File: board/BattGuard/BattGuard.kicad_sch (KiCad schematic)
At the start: 157 parts, among them J1 OQ0271510000G, J10 Conn_01x01_Pin, J11 Conn_01x01_Pin, J12 Conn_01x01_Pin, J13 Conn_01x01_Pin, J14 Conn_01x01_Pin, J15 Conn_01x01_Pin, J17 S5B-XH-A, J2 Barrel_Jack, J3 Conn_01x22_Pin, J4 Conn_01x22_Pin, J5 Conn_01x02_Pin(xt60), J6 OLED DISPLAY, J7 EC5 JUMP CONNECTOR, J8 GSB4111312HR, J9 Conn_01x01_Pin, Q1 SIR680LDP-T1-RE3, Q2 SIR680LDP-T1-RE3, Q3 SIR680LDP-T1-RE3, Q4 SIR680LDP-T1-RE3, Q7 AO3401A, Q8 2N7002, Q9 AO3401A, SW1 SW_Push, SW2 SW_Push, U1 BQ25756ERRVR, U2 LMR51420XDDCR, U3 MCP45HV51-ST, U4 INA226, U5 LM317_TO3, U6 TLV76133KVUR, U7 TLV61047DDC

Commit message: 10.19.2026 v2
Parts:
- removed Q9: AO3401A, Package_TO_SOT_SMD:SOT-23, symbol Transistor_FET:AO3401A
- removed R20: 100k, Resistor_SMD:R_0805_2012Metric, symbol Device:R_US
- D10, D11, D7, D8, D9: footprint TestPoint:TestPoint_Pad_1.0x1.0mm -> LED_THT:LED_D1.8mm_W1.8mm_H2.4mm_Horizontal_O1.27mm_Z4.9mm
- R19: value 100 -> 1k
- R21: value 100k -> 1K
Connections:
- net GPIO4: now also Q8.1 (G), R19.2; no longer R19.1
- net at Q7.2 (S), R21.1: now also R18.1, U5.3 (VO)
- net at C42.1, R22.1, U4.10 (Vin+): now also Q7.3 (D)
- net -BATT renamed GND
- net GND: now also R19.1
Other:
- moved on the sheet: C42, Q8, R19

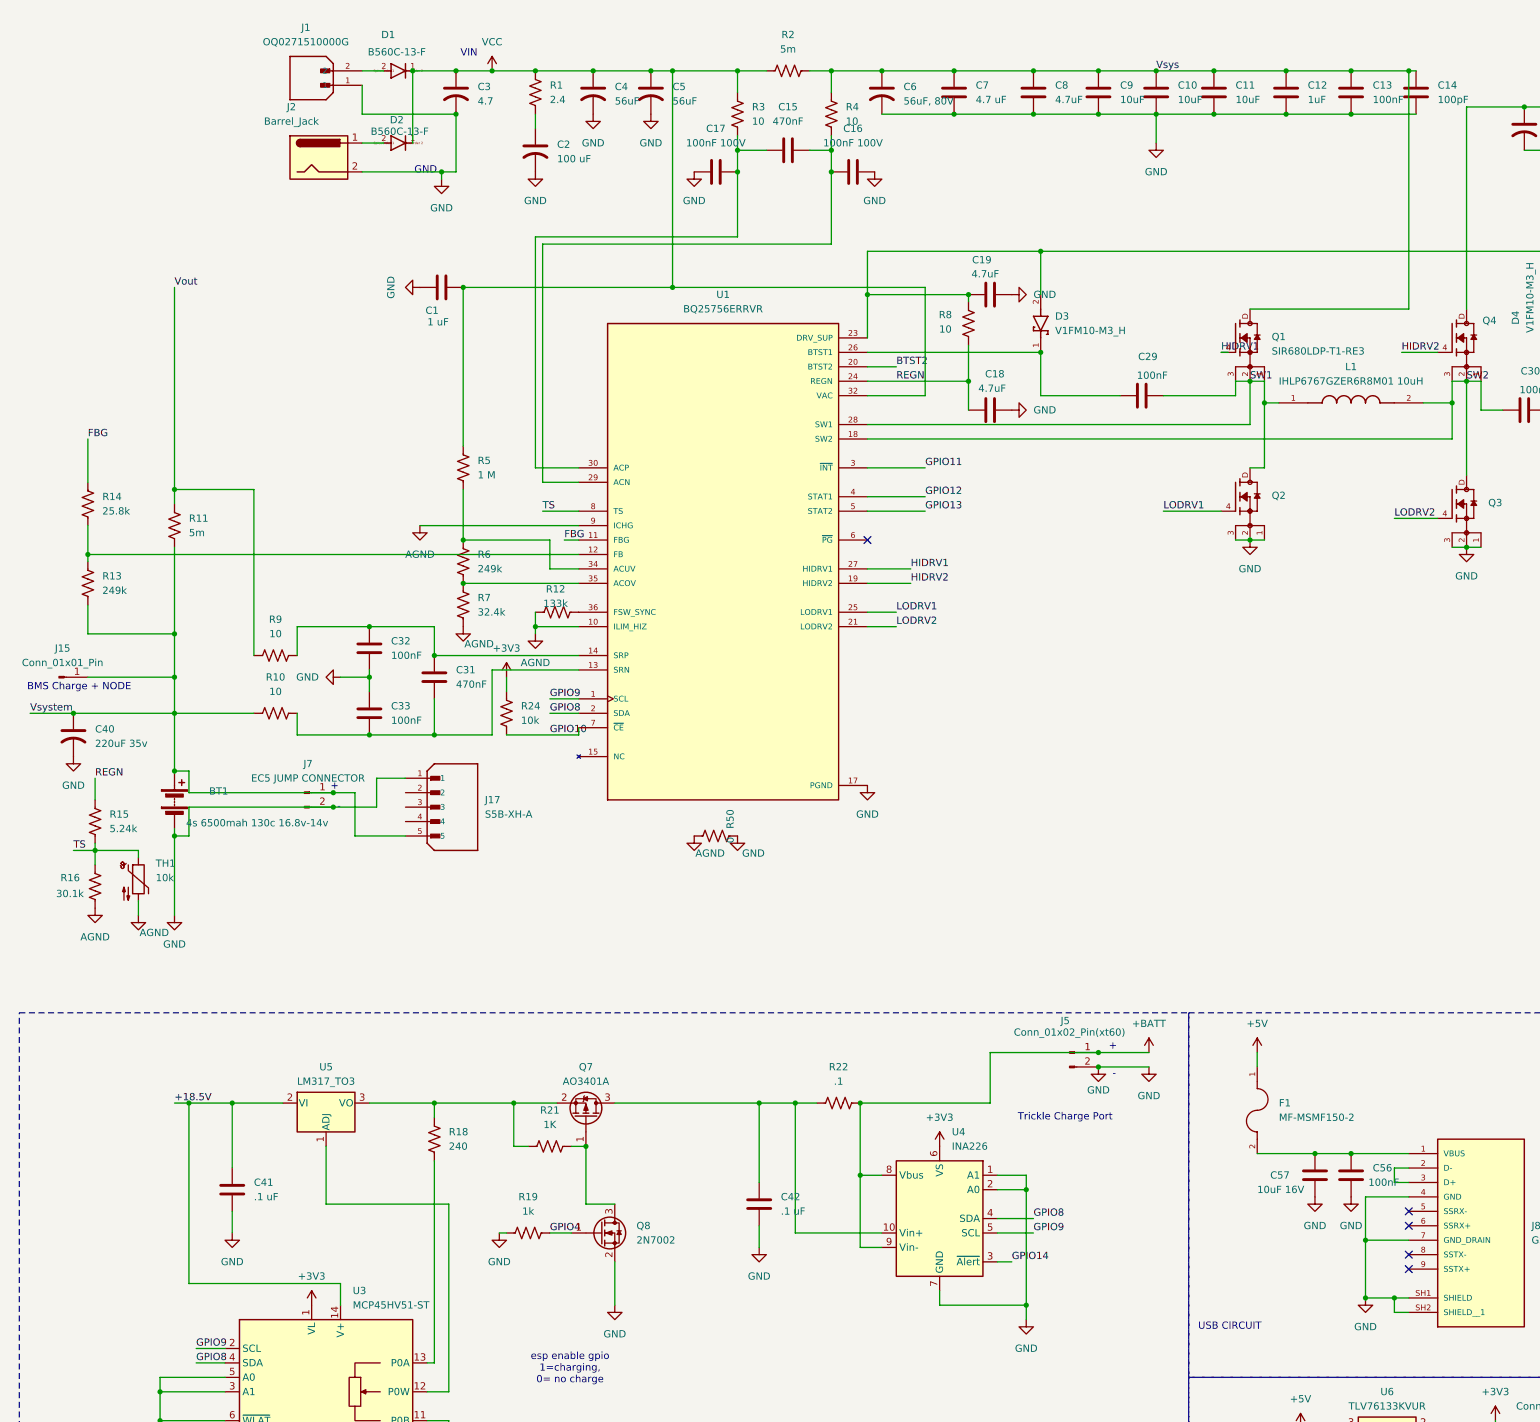
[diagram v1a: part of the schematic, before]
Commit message: Updated ESP32 Devkit, Added Input protection
Reverse polarity BQ Input protection, labeled input blocks, added model for U2
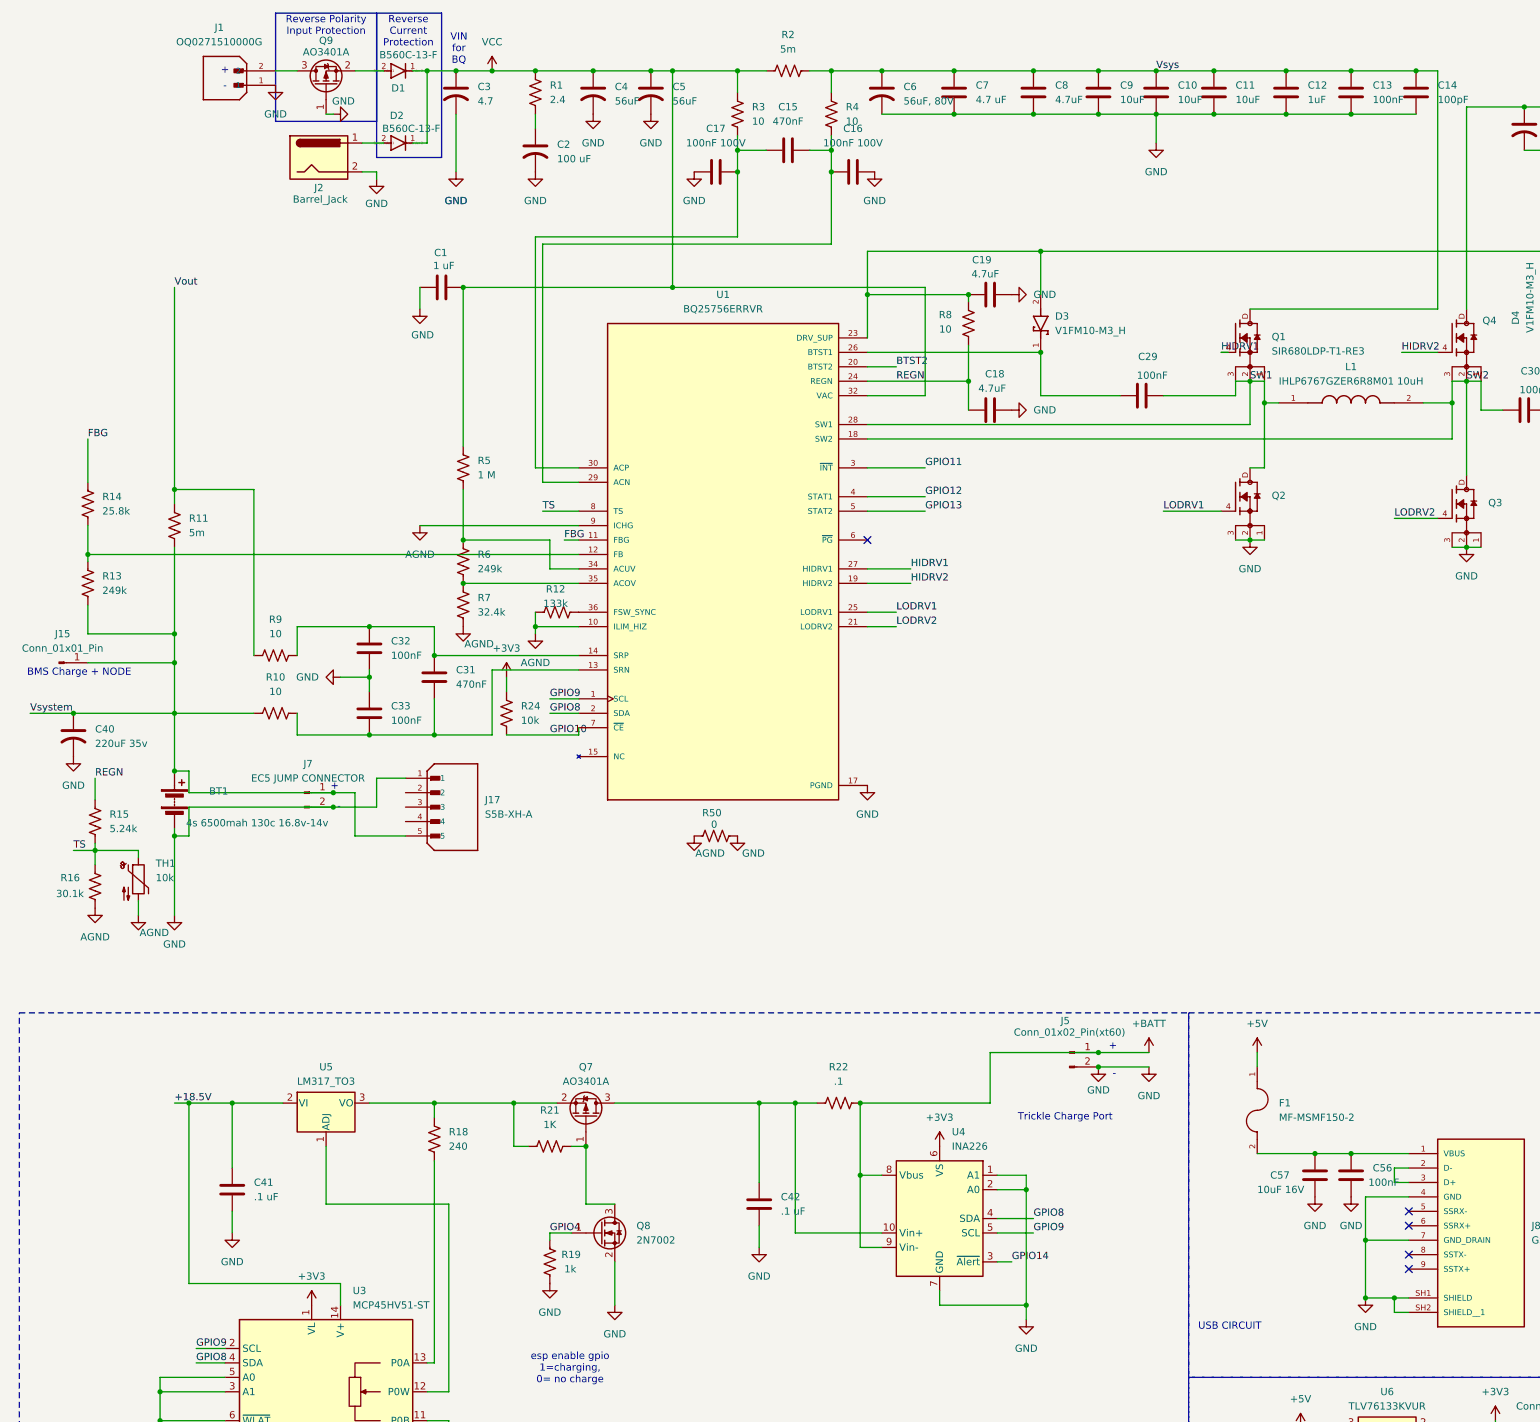
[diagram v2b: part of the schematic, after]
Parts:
- added Q9: AO3401A, Package_TO_SOT_SMD:SOT-23, symbol Transistor_FET:AO3401A
- J1: footprint BattGuard:CONN_SD-39522-003_02P_MOL -> Connector_Phoenix_GMSTB:PhoenixContact_GMSTBA_2,5_2-G_1x02_P7.50mm_Horizontal
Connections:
- net GND: now also Q9.1 (G)
- net at D1.2: now also Q9.2 (S); no longer J1.2
- new net: J1.2, Q9.3 (D)
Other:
- note added: "Reverse Current Protection"
- note added: "Reverse Polarity Input Protection"
- note added: "VIN for BQ"
- note removed: "VIN"
- moved on the sheet: J1, J15, R19

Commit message: 10.20.2026 Changes
Fixed connectors, pours, some NCs
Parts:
- R22: value .1 -> 0.05
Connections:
- net GPIO11: no longer J3.18 (Pin_18), J3.19 (Pin_19), J3.20 (Pin_20), R26.2, R27.2, R28.2, U1.4 (STAT1), U1.5 (STAT2), U4.3 (~{Alert})
- net VCC: now reaches J1.2, Q9.3 (D)
- new net GPIO12: J3.18 (Pin_18), R26.2, U1.4 (STAT1)
- new net GPIO13: J3.19 (Pin_19), R27.2, U1.5 (STAT2)
- new net GPIO14: J3.20 (Pin_20), R28.2, U4.3 (~{Alert})
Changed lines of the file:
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@@
 	(text "USB CIRCUIT\n"
 		(exclude_from_sim no)
-		(at 225.044 243.84 0)
+		(at 225.044 250.444 0)
 		(effects
 			(font
@@
 	)
 	(junction
-		(at 306.07 115.57)
-		(diameter 0)
-		(color 0 0 0 0)
-	)
-	(junction
 		(at 127 22.86)
 		(diameter 0)
@@
 	)
 	(junction
-		(at 306.07 113.03)
-		(diameter 0)
-		(color 0 0 0 0)
-	)
-	(junction
 		(at 67.31 149.86)
 		(diameter 0)
@@
 	)
 	(junction
-		(at 95.25 22.86)
-		(diameter 0)
-		(color 0 0 0 0)
-	)
-	(junction
 		(at 298.45 95.25)
 		(diameter 0)
@@
 	)
 	(junction
-		(at 306.07 110.49)
+		(at 58.42 22.86)
 		(diameter 0)
 		(color 0 0 0 0)
@@
 	)
 	(junction
-		(at 306.07 107.95)
-		(diameter 0)
-		(color 0 0 0 0)
-	)
-	(junction
 		(at 176.53 30.48)
 		(diameter 0)
@@
 	(wire
 		(pts
-			(xy 95.25 22.86) (xy 102.87 22.86)
-		)
-		(stroke
-			(width 0)
-			(type default)
-		)
-	)
-	(wire
-		(pts
 			(xy 389.89 78.74) (xy 375.92 78.74)
 		)
@@
 	(wire
 		(pts
-			(xy 306.07 113.03) (xy 306.07 115.57)
-		)
-		(stroke
-			(width 0)
-			(type default)
-		)
-	)
-	(wire
-		(pts
 			(xy 356.87 226.06) (xy 383.54 226.06)
 		)
@@
 	(wire
 		(pts
-			(xy 57.15 22.86) (xy 60.96 22.86)
+			(xy 57.15 22.86) (xy 58.42 22.86)
 		)
 		(stroke
@@
 	(wire
 		(pts
-			(xy 306.07 110.49) (xy 306.07 113.03)
-		)
-		(stroke
-			(width 0)
-			(type default)
-		)
-	)
-	(wire
-		(pts
 			(xy 109.22 212.09) (xy 111.76 212.09)
 		)
@@
 	(wire
 		(pts
-			(xy 88.9 22.86) (xy 95.25 22.86)
+			(xy 88.9 22.86) (xy 102.87 22.86)
 		)
 		(stroke
@@
 	(wire
 		(pts
-			(xy 36.83 252.73) (xy 36.83 255.27)
+			(xy 58.42 22.86) (xy 60.96 22.86)
 		)
 		(stroke
@@
 	(wire
 		(pts
-			(xy 373.38 194.31) (xy 379.73 194.31)
+			(xy 36.83 252.73) (xy 36.83 255.27)
 		)
 		(stroke
@@
 	(wire
 		(pts
-			(xy 269.24 77.47) (xy 269.24 82.55)
+			(xy 373.38 194.31) (xy 379.73 194.31)
 		)
 		(stroke
@@
 	(wire
 		(pts
-			(xy 160.02 217.17) (xy 163.83 217.17)
+			(xy 269.24 77.47) (xy 269.24 82.55)
 		)
 		(stroke
@@
 	(wire
 		(pts
-			(xy 401.32 194.31) (xy 397.51 194.31)
+			(xy 160.02 217.17) (xy 163.83 217.17)
 		)
 		(stroke
@@
 	(wire
 		(pts
-			(xy 68.58 240.03) (xy 68.58 236.22)
+			(xy 401.32 194.31) (xy 397.51 194.31)
 		)
 		(stroke
@@
 	(wire
 		(pts
-			(xy 306.07 107.95) (xy 306.07 110.49)
+			(xy 68.58 240.03) (xy 68.58 236.22)
 		)
 		(stroke
@@
 	)
 	(symbol
-		(lib_id "power:VCC")
-		(at 95.25 22.86 0)
-		(unit 1)
-		(body_style 1)
-		(exclude_from_sim no)
-		(in_bom yes)
-		(on_board yes)
-		(in_pos_files yes)
-		(dnp no)
-		(fields_autoplaced yes)
-		(property "Reference" "#PWR032"
-			(at 95.25 26.67 0)
-			(hide yes)
-			(show_name no)
-			(do_not_autoplace no)
-			(effects
-				(font
-					(size 1.27 1.27)
-				)
-			)
-		)
-		(property "Value" "VCC"
-			(at 95.25 17.78 0)
-			(show_name no)
-			(do_not_autoplace no)
-			(effects
-				(font
-					(size 1.27 1.27)
-				)
-			)
-		)
-		(property "Footprint" ""
-			(at 95.25 22.86 0)
-			(hide yes)
-			(show_name no)
-			(do_not_autoplace no)
-			(effects
-				(font
-					(size 1.27 1.27)
-				)
-			)
-		)
-		(property "Datasheet" ""
-			(at 95.25 22.86 0)
-			(hide yes)
-			(show_name no)
-			(do_not_autoplace no)
-			(effects
-				(font
-					(size 1.27 1.27)
-				)
-			)
-		)
-		(property "Description" "Power symbol creates a global label with name \"VCC\""
-			(at 95.25 22.86 0)
-			(hide yes)
-			(show_name no)
-			(do_not_autoplace no)
-			(effects
-				(font
-					(size 1.27 1.27)
-				)
-			)
-		)
-		(pin "1"
-		)
-		(instances
-			(project "BattGuard"
-				(path "/236cbdd7-d83d-4a8e-9ca8-a6b8cdb61d8b"
-					(reference "#PWR032")
-					(unit 1)
-				)
-			)
-		)
-	)
-	(symbol
 		(lib_id "power:GND")
 		(at 130.81 40.64 0)
@@
 	)
 	(symbol
+		(lib_id "power:VCC")
+		(at 58.42 22.86 0)
+		(unit 1)
+		(body_style 1)
+		(exclude_from_sim no)
+		(in_bom yes)
+		(on_board yes)
+		(in_pos_files yes)
+		(dnp no)
+		(fields_autoplaced yes)
+		(property "Reference" "#PWR032"
+			(at 58.42 26.67 0)
+			(hide yes)
+			(show_name no)
+			(do_not_autoplace no)
+			(effects
+				(font
+					(size 1.27 1.27)
+				)
+			)
+		)
+		(property "Value" "VCC"
+			(at 58.42 17.78 0)
+			(show_name no)
+			(do_not_autoplace no)
+			(effects
+				(font
+					(size 1.27 1.27)
+				)
+			)
+		)
+		(property "Footprint" ""
+			(at 58.42 22.86 0)
+			(hide yes)
+			(show_name no)
+			(do_not_autoplace no)
+			(effects
+				(font
+					(size 1.27 1.27)
+				)
+			)
+		)
+		(property "Datasheet" ""
+			(at 58.42 22.86 0)
+			(hide yes)
+			(show_name no)
+			(do_not_autoplace no)
+			(effects
+				(font
+					(size 1.27 1.27)
+				)
+			)
+		)
+		(property "Description" "Power symbol creates a global label with name \"VCC\""
+			(at 58.42 22.86 0)
+			(hide yes)
+			(show_name no)
+			(do_not_autoplace no)
+			(effects
+				(font
+					(size 1.27 1.27)
+				)
+			)
+		)
+		(pin "1"
+		)
+		(instances
+			(project "BattGuard"
+				(path "/236cbdd7-d83d-4a8e-9ca8-a6b8cdb61d8b"
+					(reference "#PWR032")
+					(unit 1)
+				)
+			)
+		)
+	)
+	(symbol
 		(lib_id "Device:C")
 		(at 289.56 33.02 0)
@@
 			)
 		)
-		(property "Value" ".1"
+		(property "Value" "0.05"
 			(at 156.21 200.66 90)
 			(show_name no)

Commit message: 10.29.2026
fixed copper keepouts around all 4 mounting holes so the screws can’t short to the frame.
Removed J7 from the board,
Added fan pads J18 and J19
fixed polarized symbols
Changed C2 to 2.2 µF, 100 V, 1206.
BQ25756 Shifted according to checklist
Gave D3/D4 their correct small footprint.
Connected U1’s thermal vias to GND.
Re-routed the BQ area to the TI checklist:
HIDRV is 0.5 mm, paired with its SW trace.
LODRV runs on the bottom layer.
Fixed input nodes solar in, then solar_Prot(reverse protected node), and barrel in all to VCC node
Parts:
- added J18: FAN1 5V, TeamLib:Fan_Wire_Pads_1x02_SMD, symbol Connector:Conn_01x02_Pin
- added J19: FAN2 5V, TeamLib:Fan_Wire_Pads_1x02_SMD, symbol Connector:Conn_01x02_Pin
- C2: value 100 uF -> 2.2uF 100V; footprint Capacitor_SMD:C_0805_2012Metric -> Capacitor_SMD:C_1206_3216Metric
- C28, C34, C35, C4, C40, C44, C45, C5, C6: symbol Device:C_US -> Device:C_Polarized_US
- D3, D4: footprint Diode_SMD:D_SMC -> TeamLib:DIO_V1FM10-M3_H
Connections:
- net +5V: now also J18.1 (Pin_1), J19.1 (Pin_1)
- net GND: now also J18.2 (Pin_2), J19.2 (Pin_2)
- net BARREL_IN: now reaches D2.2, J2.1
- net SOLAR_PROT: now reaches D1.2, Q9.2 (S)
- net VCC renamed SOLAR_IN
